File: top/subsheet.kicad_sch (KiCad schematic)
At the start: 1 part

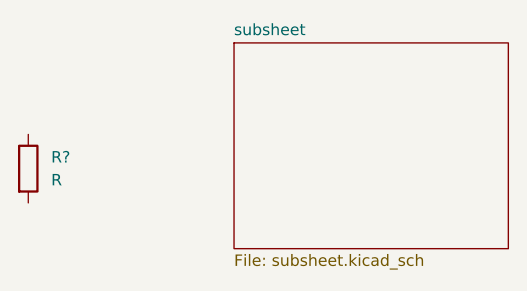
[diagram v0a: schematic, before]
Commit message: added subsheet
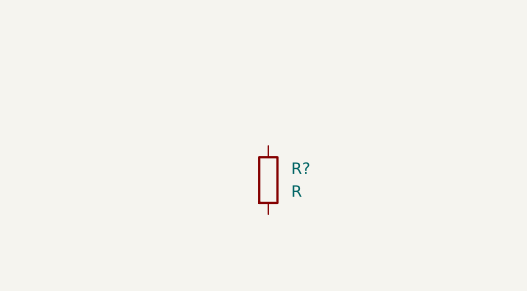
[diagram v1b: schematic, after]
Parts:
- removed R?: R, symbol Device:R
- added R?: R, symbol Device:R
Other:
- removed sheet subsheet
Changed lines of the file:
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@@
 (kicad_sch (version 20211123) (generator eeschema)
   (paper "A4")
-  (symbol (lib_id "Device:R") (at 127 100.33 0) (unit 1)
+  (symbol (lib_id "Device:R") (at 153.67 101.6 0) (unit 1)
     (in_bom yes) (on_board yes) (fields_autoplaced)
-    (property "Reference" "R?" (id 0) (at 129.54 99.0599 0)
+    (property "Reference" "R?" (id 0) (at 156.21 100.3299 0)
       (effects (font (size 1.27 1.27)) (justify left))
     )
-    (property "Value" "R" (id 1) (at 129.54 101.5999 0)
+    (property "Value" "R" (id 1) (at 156.21 102.8699 0)
       (effects (font (size 1.27 1.27)) (justify left))
     )
-    (property "Footprint" "" (id 2) (at 125.222 100.33 90)
+    (property "Footprint" "" (id 2) (at 151.892 101.6 90)
       (effects (font (size 1.27 1.27)) hide)
     )
-    (property "Datasheet" "~" (id 3) (at 127 100.33 0)
+    (property "Datasheet" "~" (id 3) (at 153.67 101.6 0)
       (effects (font (size 1.27 1.27)) hide)
     )
@@
     (pin "2")
   )
-  (sheet (at 149.86 86.36) (size 30.48 22.86) (fields_autoplaced)
-    (stroke (width 0.1524) (type solid) (color 0 0 0 0))
-    (fill (color 0 0 0 0.0000))
-    (property "Sheet name" "subsheet" (id 0) (at 149.86 85.6484 0)
-      (effects (font (size 1.27 1.27)) (justify left bottom))
-    )
-    (property "Sheet file" "subsheet.kicad_sch" (id 1) (at 149.86 109.8046 0)
-      (effects (font (size 1.27 1.27)) (justify left top))
-    )
-  )
-  (sheet_instances
-    (path "/" (page "1"))
-    (path "/ce4d26e0-43fa-468b-87fa-126cc9d765a0" (page "2"))
-  )
-  (symbol_instances
-    (path "/ce4d26e0-43fa-468b-87fa-126cc9d765a0/450038da-accc-459c-b91f-0ccc22a8e434"
-      (reference "R?") (unit 1) (value "R") (footprint "")
-    )
-    (path "/98e355a8-cded-491e-9793-b7a2f6049815"
-      (reference "R?") (unit 1) (value "R") (footprint "")
-    )
-  )
 )
